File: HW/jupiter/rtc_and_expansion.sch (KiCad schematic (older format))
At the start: 3 parts

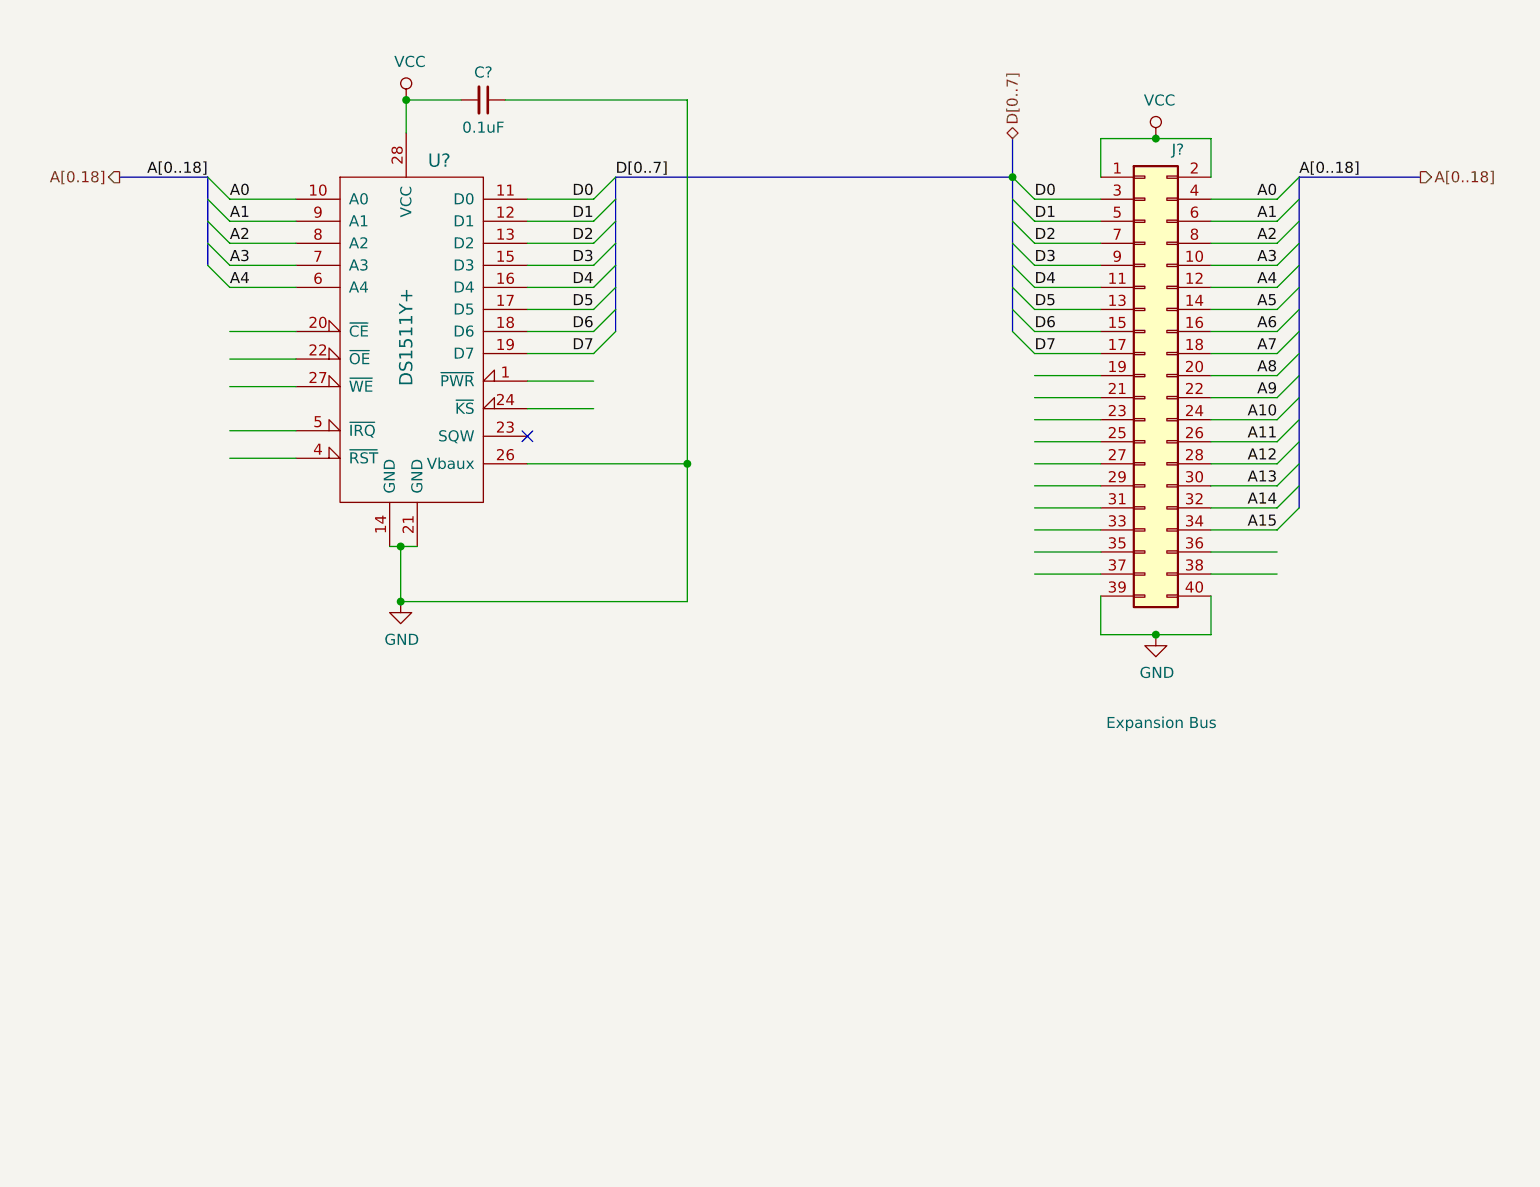
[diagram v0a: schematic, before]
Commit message: Started PCB. CPU, RTC and support section added.
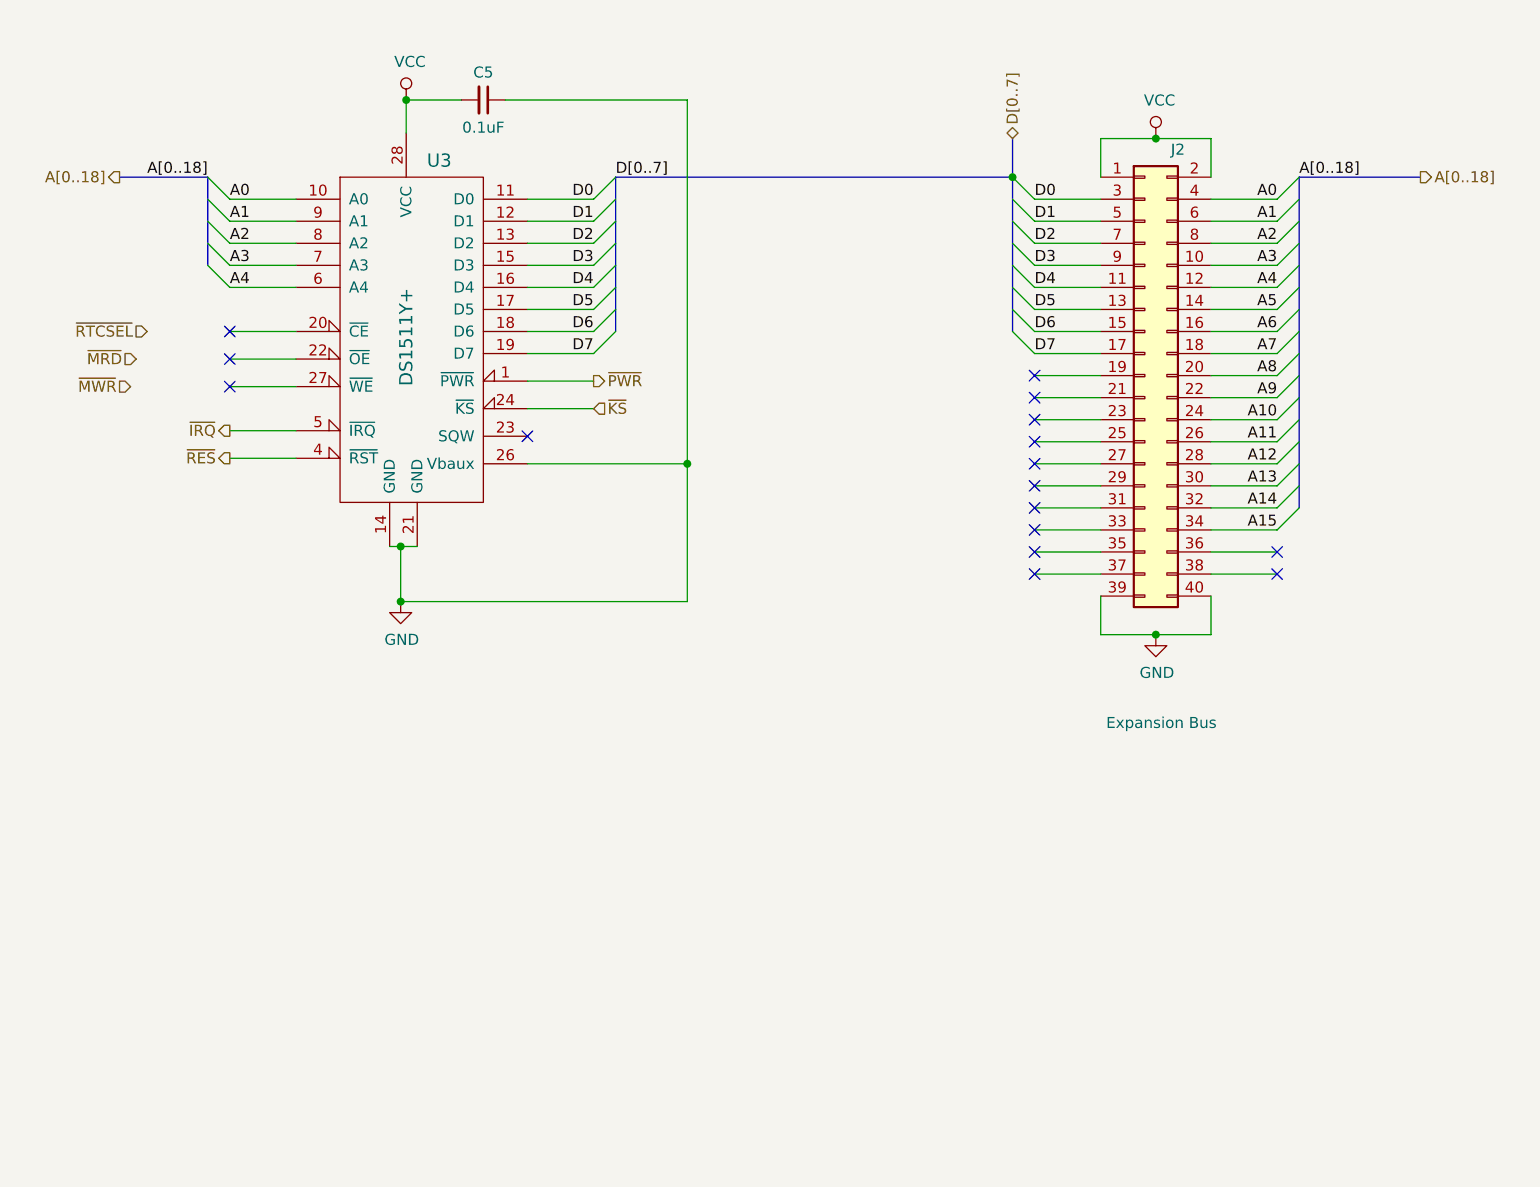
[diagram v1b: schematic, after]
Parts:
- C5: renamed from C?; footprint (none) -> Capacitor_THT:C_Disc_D4.7mm_W2.5mm_P5.00mm
- J2: renamed from J?; footprint (none) -> Connector_IDC:IDC-Header_2x20_P2.54mm_Vertical
- U3: renamed from U?; footprint (none) -> Package_DIP:DIP-28_W15.24mm_Socket
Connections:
- net labels added: ~IRQ, ~KS, ~MRD, ~MWR, ~PWR, ~RES, ~RTCSEL
- net labels removed: A[0.18]
- no-connect marks 1 -> 16
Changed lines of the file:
@@
 $Descr A4 11693 8268
 encoding utf-8
-Sheet 3 3
+Sheet 3 4
 Title ""
 Date ""
@@
 $EndDescr
 $Comp
-L Grotto:DS1511Y+ U?
+L Grotto:DS1511Y+ U3
 U 1 1 5D100309
 P 2675 2775
-F 0 "U?" H 2850 3525 60  0000 C CNN
+F 0 "U3" H 2850 3525 60  0000 C CNN
 F 1 "DS1511Y+" V 2700 2725 60  0000 C CNN
-F 2 "" H 2425 3225 60  0001 C CNN
+F 2 "Package_DIP:DIP-28_W15.24mm_Socket" H 2425 3225 60  0001 C CNN
 F 3 "" H 2425 3225 60  0001 C CNN
 	1    2675 2775
@@
 $EndComp
 $Comp
-L Connector_Generic:Conn_02x20_Odd_Even J?
+L Connector_Generic:Conn_02x20_Odd_Even J2
 U 1 1 5D101C65
 P 6050 3000
-F 0 "J?" H 6200 4025 50  0000 C CNN
+F 0 "J2" H 6200 4025 50  0000 C CNN
 F 1 "Expansion Bus" H 6125 1425 50  0000 C CNN
-F 2 "" H 6050 3000 50  0001 C CNN
+F 2 "Connector_IDC:IDC-Header_2x20_P2.54mm_Vertical" H 6050 3000 50  0001 C CNN
 F 3 "~" H 6050 3000 50  0001 C CNN
 	1    6050 3000
@@
 $EndComp
 $Comp
-L power:VCC #PWR?
+L power:VCC #PWR013
 U 1 1 5D104029
 P 6100 1925
-F 0 "#PWR?" H 6100 1775 50  0001 C CNN
+F 0 "#PWR013" H 6100 1775 50  0001 C CNN
 F 1 "VCC" H 6117 2098 50  0000 C CNN
 F 2 "" H 6100 1925 50  0001 C CNN
@@
 $EndComp
 $Comp
-L power:GND #PWR?
+L power:GND #PWR014
 U 1 1 5D104306
 P 6100 4175
-F 0 "#PWR?" H 6100 3925 50  0001 C CNN
+F 0 "#PWR014" H 6100 3925 50  0001 C CNN
 F 1 "GND" H 6105 4002 50  0000 C CNN
 F 2 "" H 6100 4175 50  0001 C CNN
@@
 A[0..18]
 Text HLabel 1400 2100 0    50   Output ~ 0
-A[0.18]
-$Comp
-L Device:C_Small C?
+A[0..18]
+$Comp
+L Device:C_Small C5
 U 1 1 5D14A5F3
 P 3050 1750
-F 0 "C?" V 2925 1750 50  0000 C CNN
+F 0 "C5" V 2925 1750 50  0000 C CNN
 F 1 "0.1uF" V 3175 1750 50  0000 C CNN
-F 2 "" H 3050 1750 50  0001 C CNN
+F 2 "Capacitor_THT:C_Disc_D4.7mm_W2.5mm_P5.00mm" H 3050 1750 50  0001 C CNN
 F 3 "~" H 3050 1750 50  0001 C CNN
 	1    3050 1750
@@
 $EndComp
 $Comp
-L power:GND #PWR?
+L power:GND #PWR011
 U 1 1 5D14AF4F
 P 2675 4025
-F 0 "#PWR?" H 2675 3775 50  0001 C CNN
+F 0 "#PWR011" H 2675 3775 50  0001 C CNN
 F 1 "GND" H 2680 3852 50  0000 C CNN
 F 2 "" H 2675 4025 50  0001 C CNN
@@
 $EndComp
 $Comp
-L power:VCC #PWR?
+L power:VCC #PWR012
 U 1 1 5D14B363
 P 2700 1750
-F 0 "#PWR?" H 2700 1600 50  0001 C CNN
+F 0 "#PWR012" H 2700 1600 50  0001 C CNN
 F 1 "VCC" H 2717 1923 50  0000 C CNN
 F 2 "" H 2700 1750 50  0001 C CNN
@@
 Wire Bus Line
 	5450 2100 5450 1925
+Connection ~ 5450 2100
+Text HLabel 1900 3250 0    50   Output ~ 0
+~IRQ
+Text HLabel 1900 3375 0    50   Output ~ 0
+~RES
+Text HLabel 3550 3025 2    50   Output ~ 0
+~PWR
+Text HLabel 3550 3150 2    50   Input ~ 0
+~KS
+Text HLabel 1450 3050 0    50   Input ~ 0
+~MWR
+Text HLabel 1475 2925 0    50   Input ~ 0
+~MRD
+Text HLabel 1525 2800 0    50   Input ~ 0
+~RTCSEL
+NoConn ~ 5550 3000
+NoConn ~ 5550 3100
+NoConn ~ 5550 3200
+NoConn ~ 5550 3300
+NoConn ~ 5550 3400
+NoConn ~ 5550 3500
+NoConn ~ 5550 3600
+NoConn ~ 5550 3700
+NoConn ~ 5550 3800
+NoConn ~ 5550 3900
+NoConn ~ 6650 3800
+NoConn ~ 6650 3900
+NoConn ~ 1900 2800
+NoConn ~ 1900 2925
+NoConn ~ 1900 3050
 Wire Bus Line
 	1800 2100 1800 2500
@@
 Wire Bus Line
 	6750 2100 6750 3600
-Connection ~ 5450 2100
 $EndSCHEMATC

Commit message: Added PCB train technical capabilities.
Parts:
- C5: footprint Capacitor_THT:C_Disc_D4.7mm_W2.5mm_P5.00mm -> Capacitor_THT:C_Disc_D3.8mm_W2.6mm_P2.50mm
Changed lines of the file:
@@
 F 0 "C5" V 2925 1750 50  0000 C CNN
 F 1 "0.1uF" V 3175 1750 50  0000 C CNN
-F 2 "Capacitor_THT:C_Disc_D4.7mm_W2.5mm_P5.00mm" H 3050 1750 50  0001 C CNN
+F 2 "Capacitor_THT:C_Disc_D3.8mm_W2.6mm_P2.50mm" H 3050 1750 50  0001 C CNN
 F 3 "~" H 3050 1750 50  0001 C CNN
 	1    3050 1750

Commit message: A lot of new data sheets. Some updates to schema and PCB layout.
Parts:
- added U?: DS1501W, symbol Grotto:DS1501W
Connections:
- net A0: now also U?.10 (A0); no longer U3.10 (A0)
- net A1: now also U?.9 (A1); no longer U3.9 (A1)
- net A2: now also U?.8 (A2); no longer U3.8 (A2)
- net A3: now also U?.7 (A3); no longer U3.7 (A3)
- net A4: now also U?.6 (A4); no longer U3.6 (A4)
- net D0: now also U?.11 (D0); no longer U3.11 (D0)
- net D1: now also U?.12 (D1); no longer U3.12 (D1)
- net D2: now also U?.13 (D2); no longer U3.13 (D2)
- net D3: now also U?.15 (D3); no longer U3.15 (D3)
- net D4: now also U?.16 (D4); no longer U3.16 (D4)
- net D5: now also U?.17 (D5); no longer U3.17 (D5)
- net D6: now also U?.18 (D6); no longer U3.18 (D6)
- net D7: now also U?.19 (D7); no longer U3.19 (D7)
- net GND: now also U?.14 (GND), U?.21 (GND), U?.23 (SQW); no longer U3.14 (GND), U3.21 (GND), U3.26 (Vbaux)
- net VCC: now also U?.28 (VCC); no longer U3.28 (VCC)
- net ~IRQ: now also U?.5 (~IRQ); no longer U3.5 (~IRQ)
- net ~KS: now also U?.24 (~KS); no longer U3.24 (~KS)
- net ~PWR: now also U?.1 (~PWR); no longer U3.1 (~PWR)
- net ~RES: now also U?.4 (~RST); no longer U3.4 (~RST)
- no-connect marks 16 -> 15
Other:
- moved on the sheet: U3
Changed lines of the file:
@@
 EESchema Schematic File Version 4
 LIBS:jupiter-cache
-EELAYER 29 0
+EELAYER 30 0
 EELAYER END
 $Descr A4 11693 8268
 encoding utf-8
-Sheet 3 4
+Sheet 3 5
 Title ""
 Date ""
@@
 L Grotto:DS1511Y+ U3
 U 1 1 5D100309
-P 2675 2775
-F 0 "U3" H 2850 3525 60  0000 C CNN
-F 1 "DS1511Y+" V 2700 2725 60  0000 C CNN
-F 2 "Package_DIP:DIP-28_W15.24mm_Socket" H 2425 3225 60  0001 C CNN
-F 3 "" H 2425 3225 60  0001 C CNN
-	1    2675 2775
+P 5250 5600
+F 0 "U3" H 5425 6350 60  0000 C CNN
+F 1 "DS1511Y+" V 5275 5550 60  0000 C CNN
+F 2 "Package_DIP:DIP-28_W15.24mm_Socket" H 5000 6050 60  0001 C CNN
+F 3 "" H 5000 6050 60  0001 C CNN
+	1    5250 5600
 	1    0    0    -1
 $EndComp
@@
 D7
 Wire Wire Line
-	3250 2200 3550 2200
-Wire Wire Line
-	3250 2300 3550 2300
-Wire Wire Line
-	3250 2400 3550 2400
-Wire Wire Line
-	3250 2500 3550 2500
-Wire Wire Line
-	3250 2600 3550 2600
-Wire Wire Line
-	3250 2700 3550 2700
-Wire Wire Line
-	3250 2800 3550 2800
-Wire Wire Line
-	3250 2900 3550 2900
-Wire Wire Line
-	3250 3025 3550 3025
-Wire Wire Line
-	3250 3150 3550 3150
+	3300 3250 3600 3250
+Wire Wire Line
+	3300 3350 3600 3350
 Wire Wire Line
 	2200 2200 1900 2200
@@
 	2200 2800 1900 2800
 Wire Wire Line
-	2200 2925 1900 2925
-Wire Wire Line
-	2200 3050 1900 3050
+	2200 2900 1900 2900
+Wire Wire Line
+	2200 3000 1900 3000
 Wire Wire Line
 	2200 3250 1900 3250
 Wire Wire Line
-	2200 3375 1900 3375
+	2200 3350 1900 3350
 Text Label 3550 2200 2    50   ~ 0
 D0
@@
 L power:GND #PWR011
 U 1 1 5D14AF4F
-P 2675 4025
-F 0 "#PWR011" H 2675 3775 50  0001 C CNN
-F 1 "GND" H 2680 3852 50  0000 C CNN
-F 2 "" H 2675 4025 50  0001 C CNN
-F 3 "" H 2675 4025 50  0001 C CNN
-	1    2675 4025
+P 2750 4375
+F 0 "#PWR011" H 2750 4125 50  0001 C CNN
+F 1 "GND" H 2755 4202 50  0000 C CNN
+F 2 "" H 2750 4375 50  0001 C CNN
+F 3 "" H 2750 4375 50  0001 C CNN
+	1    2750 4375
 	1    0    0    -1
 $EndComp
@@
 L power:VCC #PWR012
 U 1 1 5D14B363
-P 2700 1750
-F 0 "#PWR012" H 2700 1600 50  0001 C CNN
-F 1 "VCC" H 2717 1923 50  0000 C CNN
-F 2 "" H 2700 1750 50  0001 C CNN
-F 3 "" H 2700 1750 50  0001 C CNN
-	1    2700 1750
-	1    0    0    -1
-$EndComp
-Wire Wire Line
-	2700 1900 2700 1750
-Wire Wire Line
-	2700 1750 2950 1750
-Connection ~ 2700 1750
+P 2750 1600
+F 0 "#PWR012" H 2750 1450 50  0001 C CNN
+F 1 "VCC" H 2767 1773 50  0000 C CNN
+F 2 "" H 2750 1600 50  0001 C CNN
+F 3 "" H 2750 1600 50  0001 C CNN
+	1    2750 1600
+	1    0    0    -1
+$EndComp
+Wire Wire Line
+	2750 1750 2950 1750
 Wire Wire Line
 	3150 1750 3975 1750
-Wire Wire Line
-	3975 1750 3975 3400
-Wire Wire Line
-	3975 4025 2675 4025
-Wire Wire Line
-	2750 3775 2675 3775
-Wire Wire Line
-	2675 4025 2675 3775
-Connection ~ 2675 4025
-Connection ~ 2675 3775
-Wire Wire Line
-	2675 3775 2625 3775
-Wire Wire Line
-	3250 3400 3975 3400
-Connection ~ 3975 3400
-Wire Wire Line
-	3975 3400 3975 4025
-NoConn ~ 3250 3275
 Wire Bus Line
 	3650 2100 5450 2100
@@
 Text HLabel 1900 3250 0    50   Output ~ 0
 ~IRQ
-Text HLabel 1900 3375 0    50   Output ~ 0
+Text HLabel 1900 3350 0    50   Output ~ 0
 ~RES
-Text HLabel 3550 3025 2    50   Output ~ 0
+Text HLabel 3600 3250 2    50   Output ~ 0
 ~PWR
-Text HLabel 3550 3150 2    50   Input ~ 0
+Text HLabel 3600 3350 2    50   Input ~ 0
 ~KS
 Text HLabel 1450 3050 0    50   Input ~ 0
@@
 NoConn ~ 6650 3900
 NoConn ~ 1900 2800
-NoConn ~ 1900 2925
-NoConn ~ 1900 3050
+NoConn ~ 1900 2900
+NoConn ~ 1900 3000
+Wire Wire Line
+	3300 2200 3550 2200
+Wire Wire Line
+	3300 2300 3550 2300
+Wire Wire Line
+	3300 2400 3550 2400
+Wire Wire Line
+	3300 2500 3550 2500
+Wire Wire Line
+	3300 2600 3550 2600
+Wire Wire Line
+	3300 2700 3550 2700
+Wire Wire Line
+	3300 2800 3550 2800
+Wire Wire Line
+	3300 2900 3550 2900
+Wire Wire Line
+	3975 1750 3975 3450
+Wire Wire Line
+	3300 3450 3975 3450
+Wire Wire Line
+	2750 1600 2750 1750
+Wire Wire Line
+	2750 1750 2750 1850
+Connection ~ 2750 1750
+$Comp
+L Grotto:DS1501W U?
+U 1 1 5DA42BF4
+P 2750 2750
+F 0 "U?" H 2475 3500 60  0000 C CNN
+F 1 "DS1501W" V 2750 2200 60  0000 C CNN
+F 2 "" H 2450 3200 60  0001 C CNN
+F 3 "" H 2450 3200 60  0001 C CNN
+	1    2750 2750
+	1    0    0    -1
+$EndComp
+Connection ~ 3975 3450
+Wire Wire Line
+	2650 4200 2650 4300
+Wire Wire Line
+	2650 4300 2750 4300
+Wire Wire Line
+	2850 4300 2850 4200
+Wire Wire Line
+	2750 4300 2750 4375
+Connection ~ 2750 4300
+Wire Wire Line
+	2750 4300 2850 4300
+Wire Wire Line
+	3975 4300 2850 4300
+Wire Wire Line
+	3975 3450 3975 4300
+Connection ~ 2850 4300
 Wire Bus Line
 	1800 2100 1800 2500
